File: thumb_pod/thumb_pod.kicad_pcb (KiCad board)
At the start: 2 copper layers, 93 x 56 mm, 38 parts, among them J1 Conn_02x06_Odd_Even, J3 Conn_02x06_Odd_Even, SW1 SW_Push, SW10 SW_Push_SPDT, SW2 SW_Push, SW3 SW_Push, SW4 SW_Push, SW5 SW_Push, SW6 SW_Push, SW7 SW_Push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

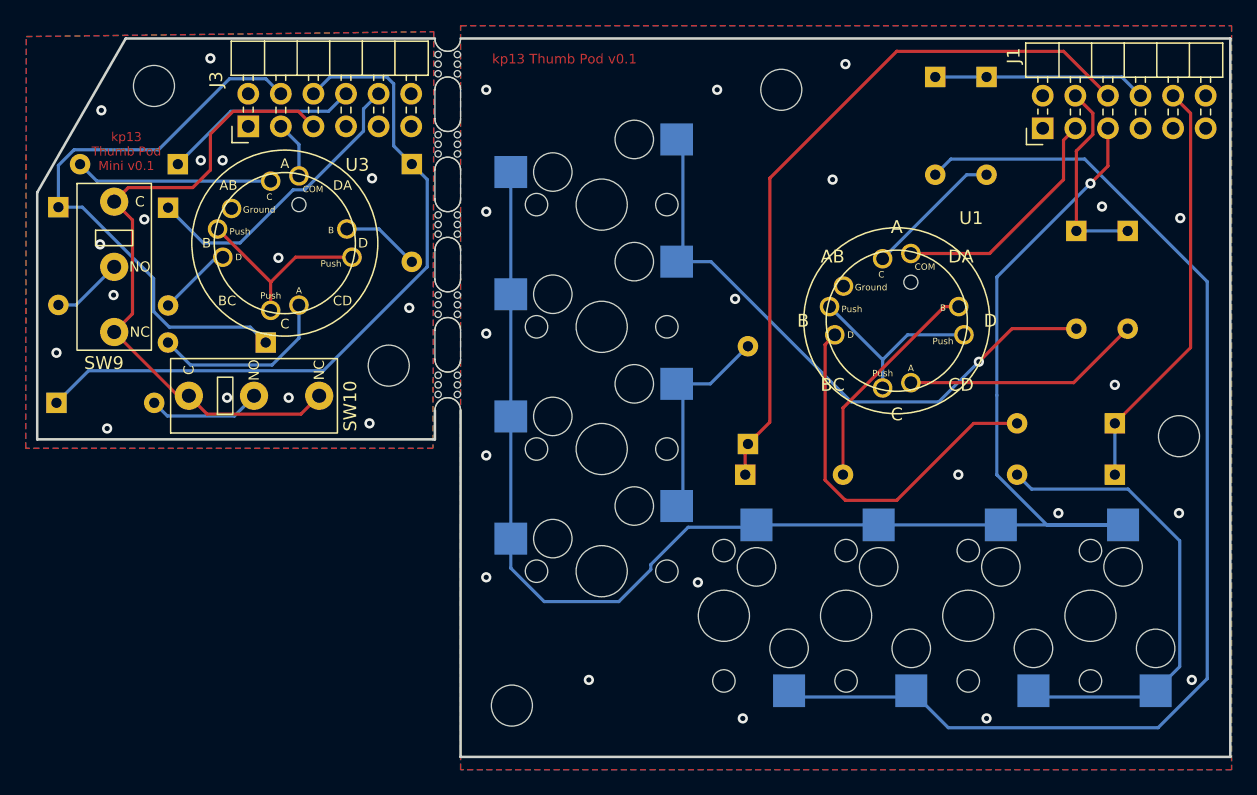
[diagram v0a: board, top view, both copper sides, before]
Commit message: - Abandoned the multi-position 1U switch experiment   - Added a notch to the thumb pod (normal sized)   - Adjusted button placement on the larger thumb pod based on testing   - Updated the readme
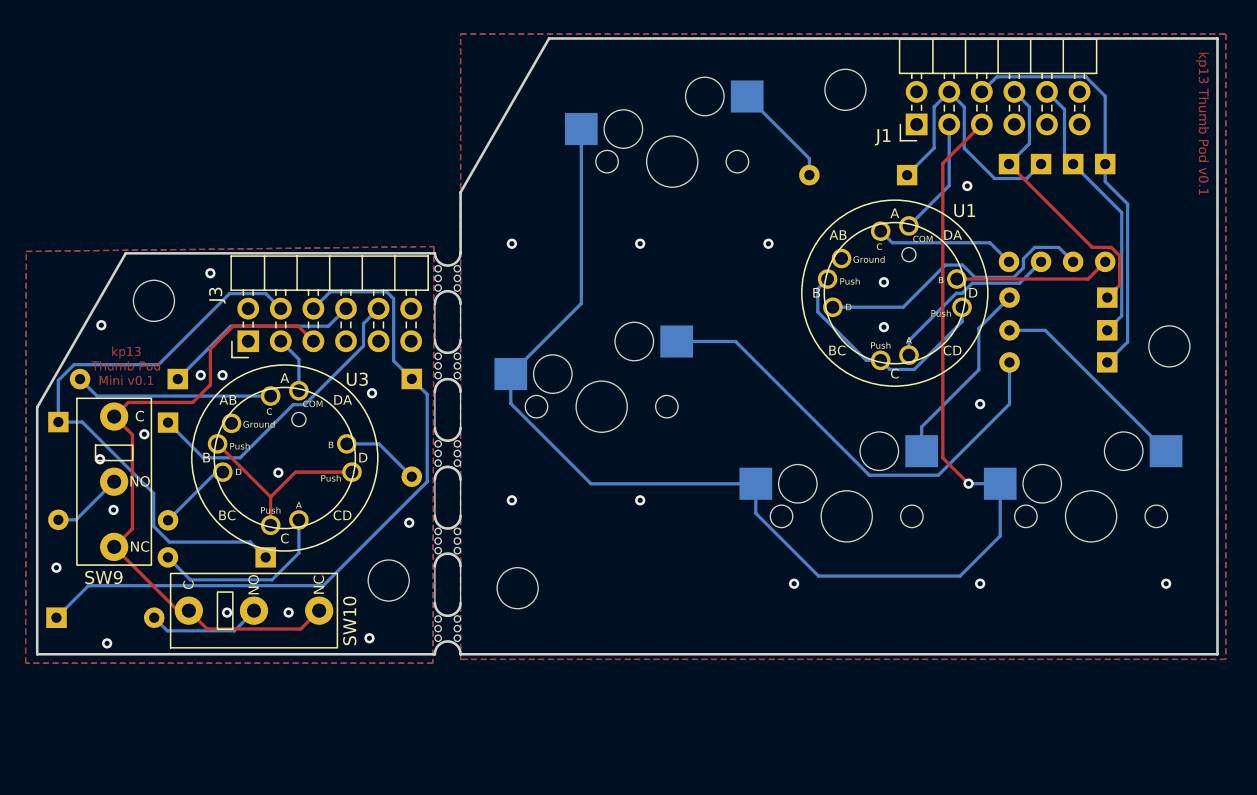
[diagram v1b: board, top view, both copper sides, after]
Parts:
- removed SW5, SW6, SW7, SW8: SW_Push, keypad:MXOnly-1U-Hotswap
- moved mouse-bite-2mm-slot 44.0 mm to (85.0, 70.0)
- moved D3 37.1 mm to (136.2, 33.8), turned to -90 degrees
- moved D4 28.7 mm to (136.4, 49.2), turned to 180 degrees
- moved D6 21.8 mm to (136.4, 44.2), turned to 180 degrees
- moved D7 20.5 mm to (133.8, 33.8), turned to -90 degrees
- moved D18 16.8 mm to (54.5, 69.2)
- moved H7 16.8 mm to (62.1, 44.5)
- moved D13 16.8 mm to (70.8, 64.5)
- moved D14 16.8 mm to (82.2, 50.5)
- moved D15 16.8 mm to (64.0, 50.5)
- moved D16 16.8 mm to (54.6, 53.9)
- moved D17 16.8 mm to (63.2, 53.9)
- moved H6 16.8 mm to (80.4, 66.2)
- moved J3 16.8 mm to (69.4, 47.6)
- moved SW9 16.8 mm to (59.0, 58.5)
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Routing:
- net Net-(D6-Pad2): track 92.4 -> 14.8 mm
- net Net-(D2-Pad2): track 48.0 -> 8.14 mm, vias 1 -> 0
- net /Col1: track 55.8 -> 32.9 mm
- net Net-(D8-Pad2): track 37.2 -> 16.1 mm
- net Net-(D4-Pad2): track 16.7 -> 35.8 mm
- net /Row5: track 124.4 -> 106.7 mm
- net /Col3: track 32.6 -> 21.5 mm
- net /Row4: track 18.7 -> 9.21 mm
- net Net-(D7-Pad2): track 29.7 -> 22.3 mm
- net /Col2: track 16.6 -> 22.0 mm
- net Net-(D3-Pad2): track 17.5 -> 12.1 mm
- net Net-(D1-Pad2): track 18.6 -> 14.0 mm
- net /Col0: track 15.6 -> 20.2 mm
- net unconnected-(U1-Pad3): track 15.5 -> 18.6 mm
- net /GND: vias 20 -> 12
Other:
- board size 93 x 56 mm -> 92 x 48 mm

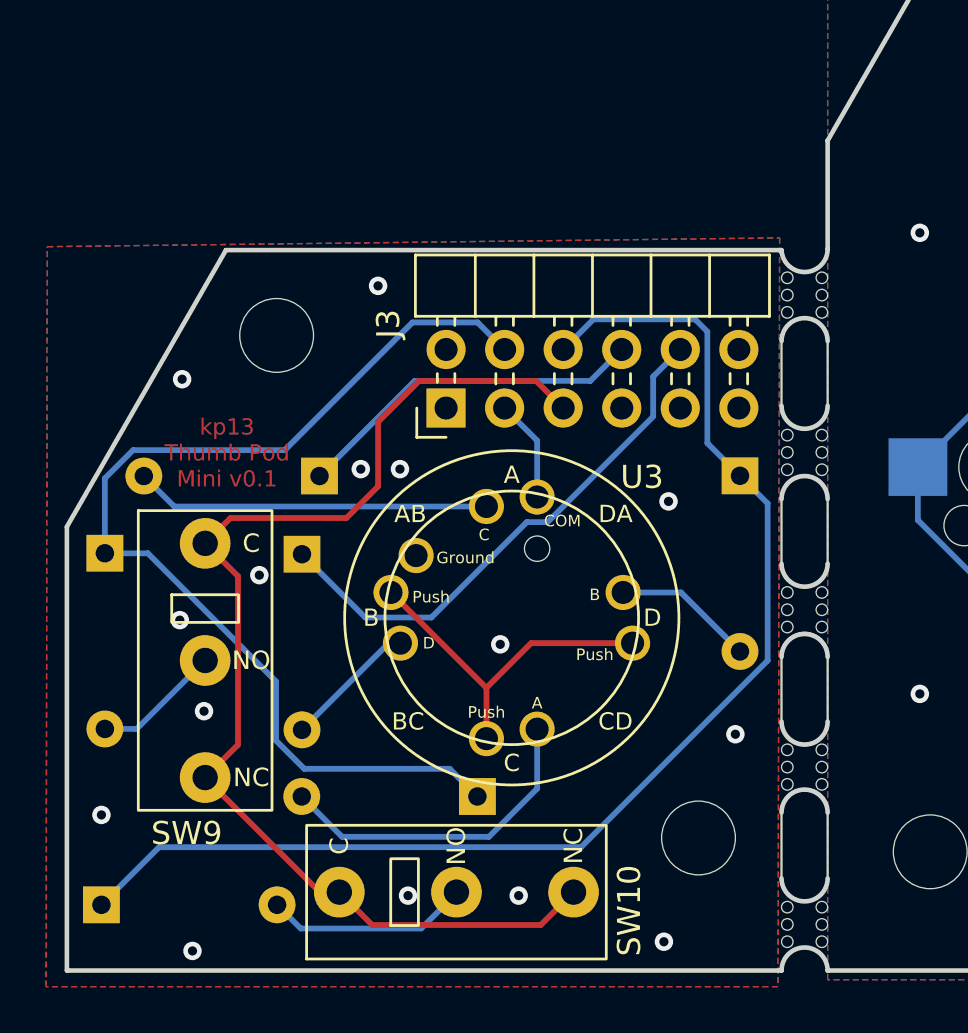
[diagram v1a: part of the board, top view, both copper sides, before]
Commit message: - Split the thumb pod PCBs
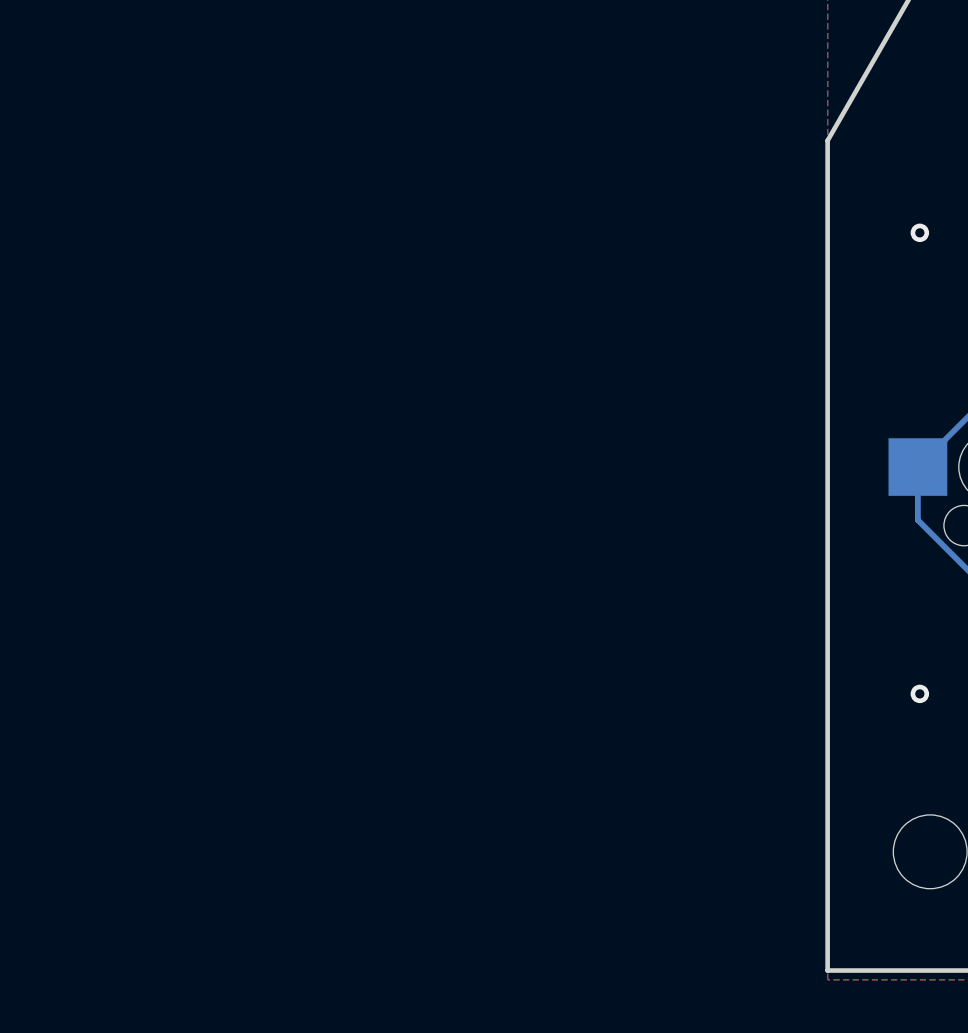
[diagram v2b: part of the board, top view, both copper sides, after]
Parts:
- removed D13, D14, D15, D16, D17, D18: 1N4148, Diode_THT:D_DO-35_SOD27_P7.62mm_Horizontal
- removed H6, H7: MountingHole, MountingHole:MountingHole_3.2mm_M3
- removed J3: Conn_02x06_Odd_Even, keypad:PinHeader_2x06_P2.54mm_Horizontal
- removed SW10, SW9: SW_Push_SPDT, keypad:kailh_gm_microswitch
- removed U3: RKJXM1015004, thumb_pod:RKJXM1015004
- removed mouse-bite-2mm-slot (x5): VAL**, thumb_pod:mouse-bite-2mm-slot
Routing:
- net Net-(D14-Pad1): track 55.7 -> 0.00 mm
- net Net-(J3-Pad5): track 51.7 -> 0.00 mm
- net Net-(D13-Pad1): track 45.9 -> 0.00 mm
- net Net-(D17-Pad1): track 23.4 -> 0.00 mm
- net Net-(D15-Pad2): track 15.4 -> 0.00 mm
- net Net-(D15-Pad1): track 15.4 -> 0.00 mm
- net unconnected-(U3-Pad3): track 15.2 -> 0.00 mm
- net Net-(D13-Pad2): track 14.4 -> 0.00 mm
- net Net-(D18-Pad2): track 8.69 -> 0.00 mm
- net Net-(D14-Pad2): track 6.13 -> 0.00 mm
- net Net-(D17-Pad2): track 5.83 -> 0.00 mm
- net Net-(D16-Pad2): track 5.58 -> 0.00 mm
- net Net-(J3-Pad3): track 4.44 -> 0.00 mm
- net /GND_m: vias 15 -> 0
- removed copper zone on B.Cu, net /GND_m
- removed copper zone on F.Cu, net /GND_m
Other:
- board size 92 x 48 mm -> 59 x 48 mm
- board text removed: "kp13 Thumb Pod Mini v0.1"
